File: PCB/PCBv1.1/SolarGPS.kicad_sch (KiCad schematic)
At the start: 54 parts, among them J1 Conn_01x10_Female, J2 Solar1+, J3 GND, J4 Conn_02x05_Odd_Even, J5 Solar2+, J6 GND, J7 Screw_Terminal_01x01, U2 MAX-M10Q, U4 STM32WB5MMGH6TR, U5 BQ25505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

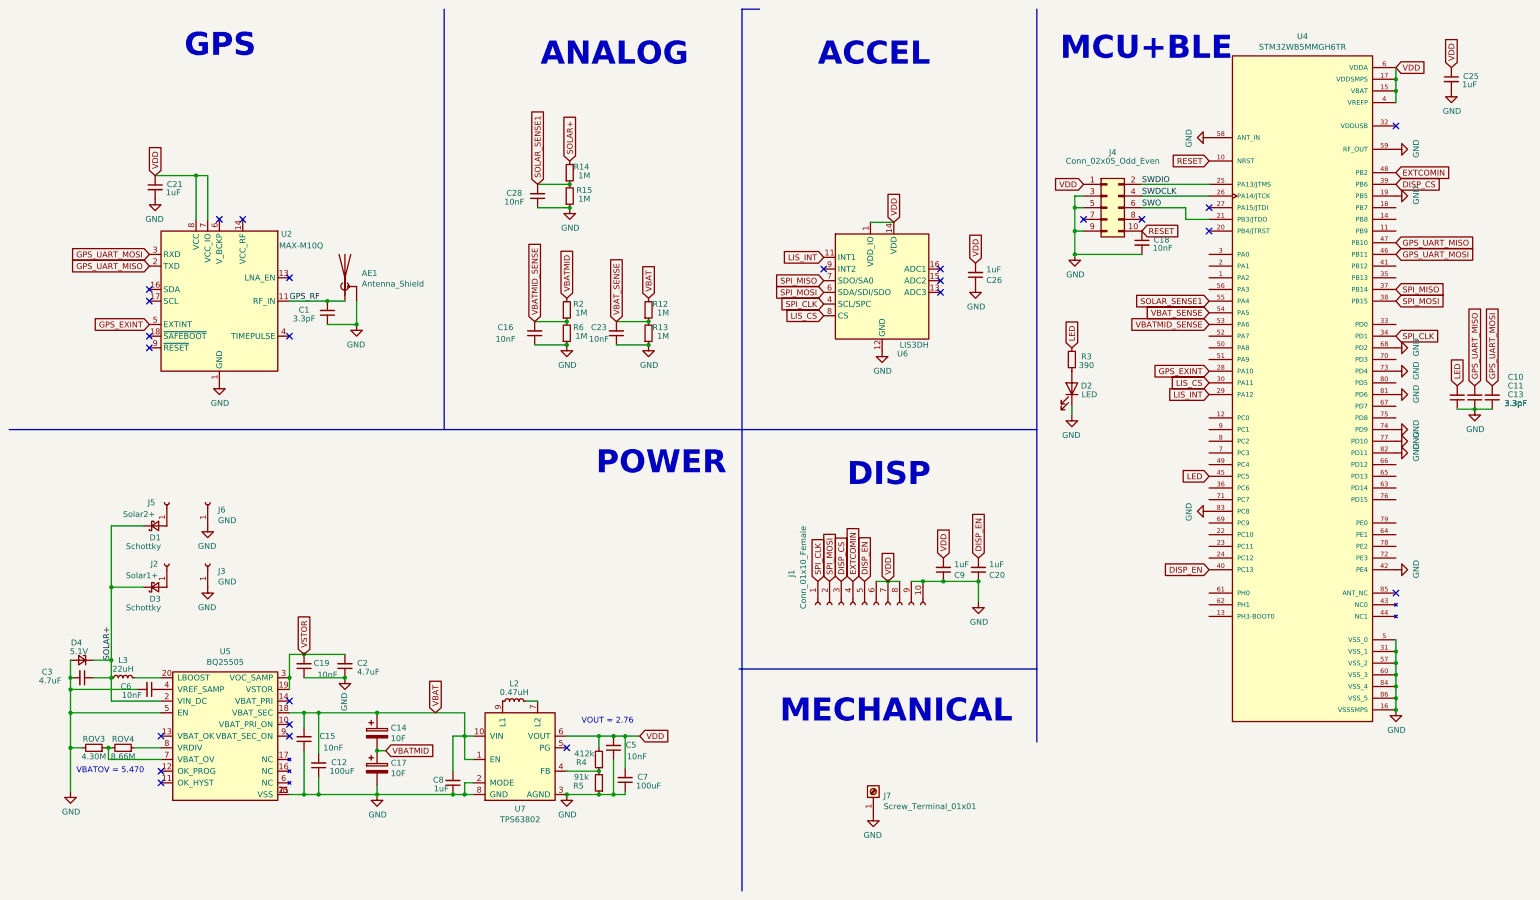
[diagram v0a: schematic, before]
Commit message: Add more App, DropBLE
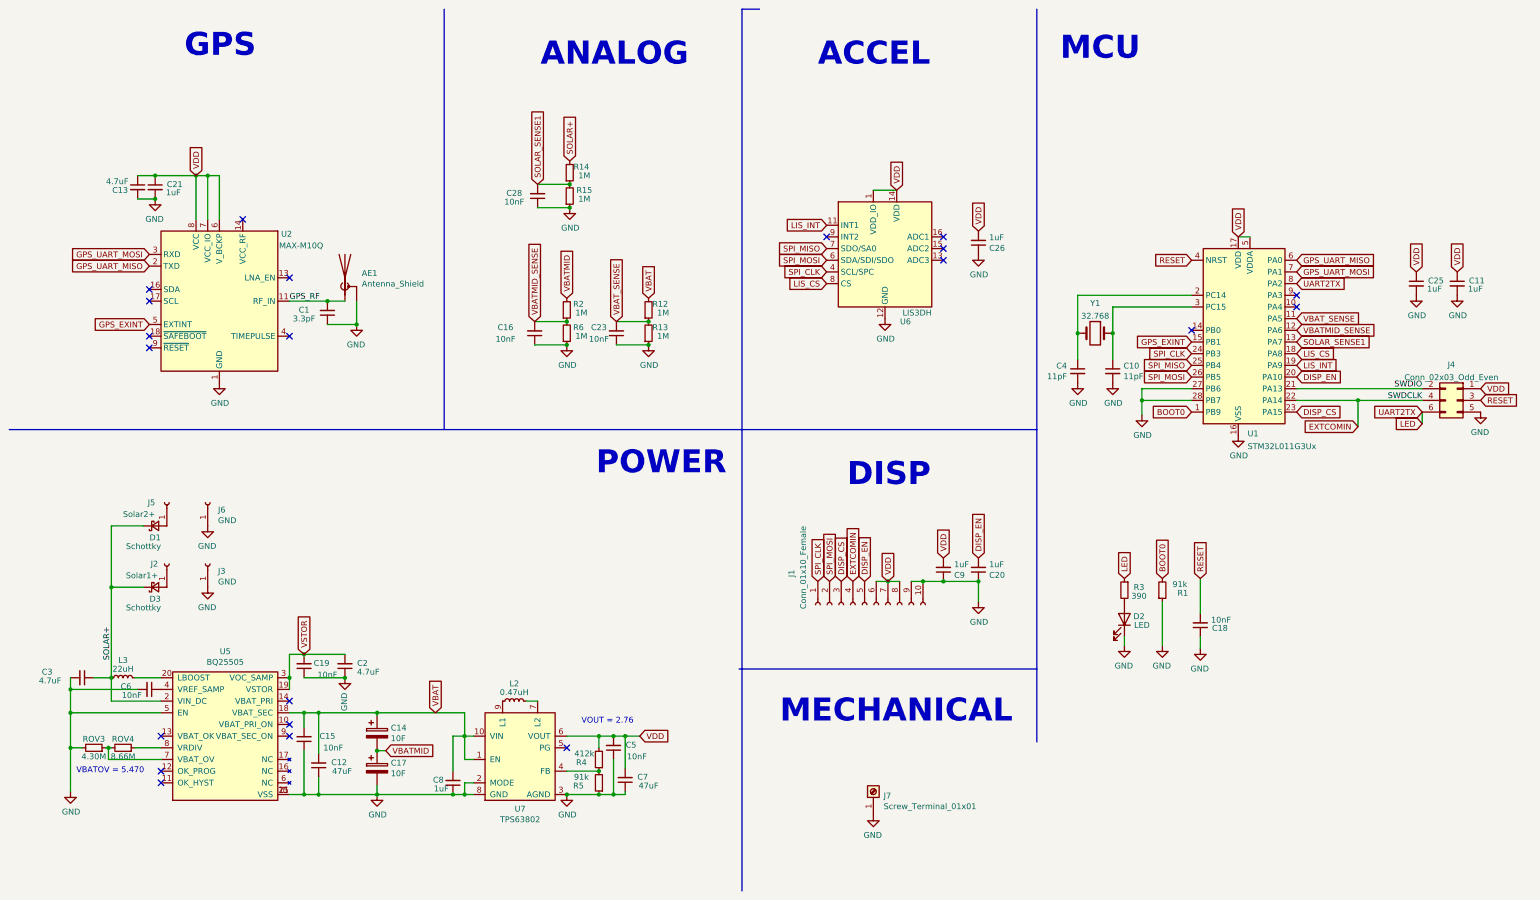
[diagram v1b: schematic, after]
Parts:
- removed D4: 5.1V, Diode_SMD:D_SOD-523, symbol Device:D_Zener_Small
- removed J4: Conn_02x05_Odd_Even, Connector_PinHeader_2.00mm:PinHeader_2x05_P2.00mm_Vertical_SMD, symbol Connector_Generic:Conn_02x05_Odd_Even
- removed U4: STM32WB5MMGH6TR, Veridian-Library-KiCad:XCVR_STM32WB5MMGH6TR, symbol SolarGPS-rescue:STM32WB5MMGH6TR-VeridianDesigns
- added C4: 11pF, Capacitor_SMD:C_0603_1608Metric, symbol Device:C_Small
- added J4: Conn_02x03_Odd_Even, Connector:Tag-Connect_TC2030-IDC-NL_2x03_P1.27mm_Vertical, symbol Connector_Generic:Conn_02x03_Odd_Even
- added R1: 91k, Resistor_SMD:R_0603_1608Metric, symbol Device:R_Small
- added U1: STM32L011G3Ux, Package_DFN_QFN:QFN-28_4x4mm_P0.5mm, symbol MCU_ST_STM32L0:STM32L011G3Ux
- added Y1: 32.768, Crystal:Crystal_SMD_3215-2Pin_3.2x1.5mm, symbol Device:Crystal
- C10: value 3.3pF -> 11pF; footprint Capacitor_SMD:C_0402_1005Metric -> Capacitor_SMD:C_0603_1608Metric
- C11: value 3.3pF -> 1uF; footprint Capacitor_SMD:C_0402_1005Metric -> Capacitor_SMD:C_0603_1608Metric
- C12, C7: value 100uF -> 47uF; footprint Capacitor_SMD:C_1206_3216Metric -> Capacitor_SMD:C_0805_2012Metric
- C13: value 3.3pF -> 4.7uF; footprint Capacitor_SMD:C_0402_1005Metric -> Capacitor_SMD:C_0805_2012Metric
- J1: footprint Margo_Lib:AYF531035 -> Margo_Lib:LS013B7DH03
- U5: footprint Package_DFN_QFN:QFN-20-1EP_3.5x3.5mm_P0.5mm_EP2x2mm_ThermalVias -> Package_DFN_QFN:QFN-20-1EP_3.5x3.5mm_P0.5mm_EP2x2mm
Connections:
- net DISP_CS: now also U1.23 (PA15)
- net DISP_EN: now also U1.20 (PA10)
- net EXTCOMIN: now also J4.4 (Pin_4), U1.22 (PA14)
- net GND: now also C10.2, C11.2, C13.2, C18.1, C4.2, J4.5 (Pin_5), R1.1, U1.16 (VSS), U1.27 (PB6), U1.28 (PB7); no longer C10.1, C11.1, C13.1, C18.2
- net GPS_EXINT: now also U1.15 (PB1)
- net GPS_UART_MISO: now also U1.6 (PA0); no longer C11.2
- net GPS_UART_MOSI: now also U1.7 (PA1); no longer C13.2
- net LED: now also J4.6 (Pin_6), U1.8 (PA2); no longer C10.2
- net LIS_CS: now also U1.18 (PA8)
- net LIS_INT: now also U1.19 (PA9)
- net RESET: now also C18.2, J4.3 (Pin_3), U1.4 (NRST); no longer C18.1
- net SOLAR_SENSE1: now also U1.13 (PA7)
- net SPI_CLK: now also U1.24 (PB3)
- net SPI_MISO: now also U1.25 (PB4)
- net SPI_MOSI: now also U1.26 (PB5)
- net SWDIO: now also J4.2 (Pin_2), U1.21 (PA13)
- net VBATMID_SENSE: now also U1.12 (PA6)
- net VBAT_SENSE: now also U1.11 (PA5)
- net VDD: now also C11.1, C13.1, U2.6 (V_BCKP), J4.1 (Pin_1), U1.17 (VDD), U1.5 (VDDA)
- new net: C4.1, U1.2 (PC14), Y1.2
- new net: C10.1, U1.3 (PC15), Y1.1
- new net BOOT0: R1.2, U1.1 (PB9)
- no-connect marks 25 -> 21
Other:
- note added: "MCU"
- note removed: "MCU+BLE"
- moved on the sheet: C18, C25, C26, D2, R3, U6

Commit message: Add some datasheets
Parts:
- R4: value 412k -> 432k
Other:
- note added: "VOUT = 2.87"
- note removed: "VOUT = 2.76"
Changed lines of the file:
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@@
   (no_connect (at 215.265 66.675))
   (no_connect (at 45.085 177.8))
+  (no_connect (at 292.1 76.835))
   (no_connect (at 215.265 64.135))
   (no_connect (at 292.1 74.295))
-  (no_connect (at 292.1 76.835))
   (no_connect (at 73.025 167.64))
   (no_connect (at 269.24 81.915))
   (no_connect (at 189.865 61.595))
-  (no_connect (at 133.35 172.72))
   (no_connect (at 73.025 170.18))
   (no_connect (at 215.265 61.595))
+  (no_connect (at 133.35 172.72))
   (no_connect (at 42.545 85.725))
   (no_connect (at 42.545 73.025))
@@
     (stroke (width 0) (type default) (color 0 0 0 0))
   )
-  (text "VOUT = 2.76" (at 136.525 167.64 0)
+  (text "VOUT = 2.87" (at 136.525 167.64 0)
     (effects (font (size 1.27 1.27)) (justify left bottom))
   )
@@
     (in_bom yes) (on_board yes)
     (property "Reference" "R4" (id 0) (at 136.525 175.895 0))
-    (property "Value" "412k" (id 1) (at 137.16 173.99 0))
+    (property "Value" "432k" (id 1) (at 137.16 173.99 0))
     (property "Footprint" "Resistor_SMD:R_0603_1608Metric" (id 2) (at 140.335 175.26 0)
       (effects (font (size 1.27 1.27)) hide)
@@
     )
     (path "/00000000-0000-0000-0000-000061ac0081"
-      (reference "R4") (unit 1) (value "412k") (footprint "Resistor_SMD:R_0603_1608Metric")
+      (reference "R4") (unit 1) (value "432k") (footprint "Resistor_SMD:R_0603_1608Metric")
     )
     (path "/00000000-0000-0000-0000-000061ae367a"

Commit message: Add custom library revise M4 mount
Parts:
- J7: footprint Veridian-Library-KiCad:Right Angle Screw Terminal M3M4 -> Heliograph:M4_RA_7792; Part 7781 -> 7792
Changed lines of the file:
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@@
       (effects (font (size 1.27 1.27)) (justify right))
     )
-    (property "Footprint" "Veridian-Library-KiCad:Right Angle Screw Terminal M3M4" (id 2) (at 200.025 182.245 0)
+    (property "Footprint" "Heliograph:M4_RA_7792" (id 2) (at 200.025 182.245 0)
       (effects (font (size 1.27 1.27)) hide)
     )
@@
       (effects (font (size 1.27 1.27)) hide)
     )
-    (property "Part" "7781" (id 4) (at 200.025 182.245 90)
+    (property "Part" "7792" (id 4) (at 200.025 182.245 90)
       (effects (font (size 1.27 1.27)) hide)
     )
@@
     )
     (path "/00000000-0000-0000-0000-000061db9c44"
-      (reference "J7") (unit 1) (value "Screw_Terminal_01x01") (footprint "Veridian-Library-KiCad:Right Angle Screw Terminal M3M4")
+      (reference "J7") (unit 1) (value "Screw_Terminal_01x01") (footprint "Heliograph:M4_RA_7792")
     )
     (path "/00000000-0000-0000-0000-000061a9953b"

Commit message: Update PCB 1.1
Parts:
- C12, C7: footprint Capacitor_SMD:C_0805_2012Metric -> Capacitor_SMD:C_1206_3216Metric
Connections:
- net GND: no longer U1.28 (PB7)
- no-connect marks 21 -> 22
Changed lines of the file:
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@@
   (junction (at 43.815 53.34) (diameter 0) (color 0 0 0 0)
-  )
-  (junction (at 258.445 97.155) (diameter 0) (color 0 0 0 0)
   )
   (junction (at 76.2 182.88) (diameter 0) (color 0 0 0 0)
@@
   (no_connect (at 215.265 64.135))
   (no_connect (at 292.1 74.295))
+  (no_connect (at 269.24 97.155))
   (no_connect (at 73.025 167.64))
   (no_connect (at 269.24 81.915))
@@
     (stroke (width 0) (type default) (color 0 0 0 0))
   )
-  (wire (pts (xy 269.24 97.155) (xy 258.445 97.155))
-    (stroke (width 0) (type default) (color 0 0 0 0))
-  )
   (wire (pts (xy 111.125 182.88) (xy 113.03 182.88))
     (stroke (width 0) (type default) (color 0 0 0 0))
@@
     (stroke (width 0) (type default) (color 0 0 0 0))
   )
-  (wire (pts (xy 258.445 97.155) (xy 258.445 100.33))
-    (stroke (width 0) (type default) (color 0 0 0 0))
-  )
   (wire (pts (xy 76.2 165.1) (xy 76.2 168.275))
     (stroke (width 0) (type default) (color 0 0 0 0))
@@
     (stroke (width 0) (type default) (color 0 0 0 0))
   )
-  (wire (pts (xy 258.445 94.615) (xy 258.445 97.155))
+  (wire (pts (xy 258.445 94.615) (xy 258.445 100.33))
     (stroke (width 0) (type default) (color 0 0 0 0))
   )
@@
     (property "Reference" "C12" (id 0) (at 83.82 175.895 0))
     (property "Value" "47uF" (id 1) (at 84.455 177.8 0))
-    (property "Footprint" "Capacitor_SMD:C_0805_2012Metric" (id 2) (at 79.375 176.53 0)
+    (property "Footprint" "Capacitor_SMD:C_1206_3216Metric" (id 2) (at 79.375 176.53 0)
       (effects (font (size 1.27 1.27)) hide)
     )
@@
     (property "Reference" "C7" (id 0) (at 149.86 179.07 0))
     (property "Value" "47uF" (id 1) (at 151.13 180.975 0))
-    (property "Footprint" "Capacitor_SMD:C_0805_2012Metric" (id 2) (at 146.05 179.705 0)
+    (property "Footprint" "Capacitor_SMD:C_1206_3216Metric" (id 2) (at 146.05 179.705 0)
       (effects (font (size 1.27 1.27)) hide)
     )
@@
     )
     (path "/00000000-0000-0000-0000-000061af5036"
-      (reference "C7") (unit 1) (value "47uF") (footprint "Capacitor_SMD:C_0805_2012Metric")
+      (reference "C7") (unit 1) (value "47uF") (footprint "Capacitor_SMD:C_1206_3216Metric")
     )
     (path "/00000000-0000-0000-0000-000061ba52ab"
@@
     )
     (path "/00000000-0000-0000-0000-000061957471"
-      (reference "C12") (unit 1) (value "47uF") (footprint "Capacitor_SMD:C_0805_2012Metric")
+      (reference "C12") (unit 1) (value "47uF") (footprint "Capacitor_SMD:C_1206_3216Metric")
     )
     (path "/9b88f61c-18a3-402d-bc49-08320c270f61"

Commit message: Tweak PCB
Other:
- moved on the sheet: C10, C4, Y1
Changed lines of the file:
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@@
   (junction (at 76.2 165.1) (diameter 0) (color 0 0 0 0)
   )
-  (junction (at 244.475 82.55) (diameter 0) (color 0 0 0 0)
-  )
   (junction (at 25.4 160.02) (diameter 0) (color 0 0 0 0)
   )
@@
   (junction (at 43.815 48.26) (diameter 0) (color 0 0 0 0)
   )
+  (junction (at 252.095 77.47) (diameter 0) (color 0 0 0 0)
+  )
   (junction (at 55.245 48.26) (diameter 0) (color 0 0 0 0)
   )
   (junction (at 140.335 177.8) (diameter 0) (color 0 0 0 0)
   )
+  (junction (at 244.475 77.47) (diameter 0) (color 0 0 0 0)
+  )
   (junction (at 203.2 136.525) (diameter 0) (color 0 0 0 0)
   )
@@
   )
   (junction (at 87.63 80.645) (diameter 0) (color 0 0 0 0)
-  )
-  (junction (at 252.095 82.55) (diameter 0) (color 0 0 0 0)
   )
   (junction (at 34.29 157.48) (diameter 0) (color 0 0 0 0)
@@
     (stroke (width 0) (type default) (color 0 0 0 0))
   )
-  (wire (pts (xy 244.475 88.265) (xy 244.475 82.55))
-    (stroke (width 0) (type default) (color 0 0 0 0))
-  )
   (wire (pts (xy 52.705 48.26) (xy 55.245 48.26))
     (stroke (width 0) (type default) (color 0 0 0 0))
@@
     (stroke (width 0) (type default) (color 0 0 0 0))
   )
-  (wire (pts (xy 244.475 74.295) (xy 244.475 82.55))
-    (stroke (width 0) (type default) (color 0 0 0 0))
-  )
   (wire (pts (xy 52.705 48.26) (xy 43.815 48.26))
     (stroke (width 0) (type default) (color 0 0 0 0))
@@
     (stroke (width 0) (type default) (color 0 0 0 0))
   )
+  (wire (pts (xy 244.475 74.295) (xy 244.475 77.47))
+    (stroke (width 0) (type default) (color 0 0 0 0))
+  )
   (wire (pts (xy 258.445 94.615) (xy 269.24 94.615))
     (stroke (width 0) (type default) (color 0 0 0 0))
@@
     (stroke (width 0) (type default) (color 0 0 0 0))
   )
+  (wire (pts (xy 252.095 77.47) (xy 252.095 80.01))
+    (stroke (width 0) (type default) (color 0 0 0 0))
+  )
   (wire (pts (xy 92.075 182.88) (xy 108.585 182.88))
     (stroke (width 0) (type default) (color 0 0 0 0))
@@
     (stroke (width 0) (type default) (color 0 0 0 0))
   )
-  (wire (pts (xy 252.095 82.55) (xy 252.095 76.835))
+  (wire (pts (xy 252.095 76.835) (xy 252.095 77.47))
     (stroke (width 0) (type default) (color 0 0 0 0))
   )
@@
     (stroke (width 0) (type default) (color 0 0 0 0))
   )
-  (wire (pts (xy 252.095 88.265) (xy 252.095 82.55))
+  (wire (pts (xy 244.475 77.47) (xy 244.475 80.01))
     (stroke (width 0) (type default) (color 0 0 0 0))
   )
@@
     (pin "2")
   )
-  (symbol (lib_id "power:GND") (at 252.095 93.345 0) (unit 1)
-    (in_bom yes) (on_board yes)
-    (property "Reference" "#PWR0110" (id 0) (at 252.095 99.695 0)
-      (effects (font (size 1.27 1.27)) hide)
-    )
-    (property "Value" "GND" (id 1) (at 252.222 97.7392 0))
-    (property "Footprint" "" (id 2) (at 252.095 93.345 0)
-      (effects (font (size 1.27 1.27)) hide)
-    )
-    (property "Datasheet" "" (id 3) (at 252.095 93.345 0)
-      (effects (font (size 1.27 1.27)) hide)
-    )
-    (pin "1")
-  )
-  (symbol (lib_id "Device:C_Small") (at 244.475 90.805 0) (mirror y) (unit 1)
-    (in_bom yes) (on_board yes)
-    (property "Reference" "C4" (id 0) (at 242.1382 89.6366 0)
-      (effects (font (size 1.27 1.27)) (justify left))
-    )
-    (property "Value" "11pF" (id 1) (at 242.1382 91.948 0)
-      (effects (font (size 1.27 1.27)) (justify left))
-    )
-    (property "Footprint" "Capacitor_SMD:C_0603_1608Metric" (id 2) (at 244.475 90.805 0)
-      (effects (font (size 1.27 1.27)) hide)
-    )
-    (property "Datasheet" "~" (id 3) (at 244.475 90.805 0)
-      (effects (font (size 1.27 1.27)) hide)
-    )
-    (pin "1")
-    (pin "2")
-  )
-  (symbol (lib_id "Device:Crystal") (at 248.285 82.55 0) (mirror y) (unit 1)
-    (in_bom yes) (on_board yes) (fields_autoplaced)
-    (property "Reference" "Y1" (id 0) (at 248.285 76.0181 0))
-    (property "Value" "32.768" (id 1) (at 248.285 78.7932 0))
-    (property "Footprint" "Crystal:Crystal_SMD_3215-2Pin_3.2x1.5mm" (id 2) (at 248.285 82.55 0)
-      (effects (font (size 1.27 1.27)) hide)
-    )
-    (property "Datasheet" "~" (id 3) (at 248.285 82.55 0)
-      (effects (font (size 1.27 1.27)) hide)
-    )
-    (property "Part" "SC32S-7PF20PPM" (id 4) (at 248.285 82.55 0)
+  (symbol (lib_id "power:GND") (at 252.095 85.09 0) (unit 1)
+    (in_bom yes) (on_board yes)
+    (property "Reference" "#PWR0110" (id 0) (at 252.095 91.44 0)
+      (effects (font (size 1.27 1.27)) hide)
+    )
+    (property "Value" "GND" (id 1) (at 252.222 89.4842 0))
+    (property "Footprint" "" (id 2) (at 252.095 85.09 0)
+      (effects (font (size 1.27 1.27)) hide)
+    )
+    (property "Datasheet" "" (id 3) (at 252.095 85.09 0)
+      (effects (font (size 1.27 1.27)) hide)
+    )
+    (pin "1")
+  )
+  (symbol (lib_id "Device:C_Small") (at 244.475 82.55 0) (mirror y) (unit 1)
+    (in_bom yes) (on_board yes)
+    (property "Reference" "C4" (id 0) (at 241.3 81.28 0)
+      (effects (font (size 1.27 1.27)) (justify left))
+    )
+    (property "Value" "11pF" (id 1) (at 242.57 83.185 0)
+      (effects (font (size 1.27 1.27)) (justify left))
+    )
+    (property "Footprint" "Capacitor_SMD:C_0603_1608Metric" (id 2) (at 244.475 82.55 0)
+      (effects (font (size 1.27 1.27)) hide)
+    )
+    (property "Datasheet" "~" (id 3) (at 244.475 82.55 0)
+      (effects (font (size 1.27 1.27)) hide)
+    )
+    (pin "1")
+    (pin "2")
+  )
+  (symbol (lib_id "Device:Crystal") (at 248.285 77.47 0) (mirror y) (unit 1)
+    (in_bom yes) (on_board yes)
+    (property "Reference" "Y1" (id 0) (at 248.285 70.9381 0))
+    (property "Value" "32.768" (id 1) (at 248.285 73.025 0))
+    (property "Footprint" "Crystal:Crystal_SMD_3215-2Pin_3.2x1.5mm" (id 2) (at 248.285 77.47 0)
+      (effects (font (size 1.27 1.27)) hide)
+    )
+    (property "Datasheet" "~" (id 3) (at 248.285 77.47 0)
+      (effects (font (size 1.27 1.27)) hide)
+    )
+    (property "Part" "SC32S-7PF20PPM" (id 4) (at 248.285 77.47 0)
       (effects (font (size 1.27 1.27)) hide)
     )
@@
     (pin "2")
   )
-  (symbol (lib_id "Device:C_Small") (at 252.095 90.805 0) (unit 1)
-    (in_bom yes) (on_board yes)
-    (property "Reference" "C10" (id 0) (at 254.4318 89.6366 0)
-      (effects (font (size 1.27 1.27)) (justify left))
-    )
-    (property "Value" "11pF" (id 1) (at 254.4318 91.948 0)
-      (effects (font (size 1.27 1.27)) (justify left))
-    )
-    (property "Footprint" "Capacitor_SMD:C_0603_1608Metric" (id 2) (at 252.095 90.805 0)
-      (effects (font (size 1.27 1.27)) hide)
-    )
-    (property "Datasheet" "~" (id 3) (at 252.095 90.805 0)
+  (symbol (lib_id "Device:C_Small") (at 252.095 82.55 0) (unit 1)
+    (in_bom yes) (on_board yes)
+    (property "Reference" "C10" (id 0) (at 254 80.01 0)
+      (effects (font (size 1.27 1.27)) (justify left))
+    )
+    (property "Value" "11pF" (id 1) (at 254 81.915 0)
+      (effects (font (size 1.27 1.27)) (justify left))
+    )
+    (property "Footprint" "Capacitor_SMD:C_0603_1608Metric" (id 2) (at 252.095 82.55 0)
+      (effects (font (size 1.27 1.27)) hide)
+    )
+    (property "Datasheet" "~" (id 3) (at 252.095 82.55 0)
       (effects (font (size 1.27 1.27)) hide)
     )
@@
     (pin "1")
   )
-  (symbol (lib_id "power:GND") (at 244.475 93.345 0) (unit 1)
-    (in_bom yes) (on_board yes)
-    (property "Reference" "#PWR0108" (id 0) (at 244.475 99.695 0)
-      (effects (font (size 1.27 1.27)) hide)
-    )
-    (property "Value" "GND" (id 1) (at 244.602 97.7392 0))
-    (property "Footprint" "" (id 2) (at 244.475 93.345 0)
-      (effects (font (size 1.27 1.27)) hide)
-    )
-    (property "Datasheet" "" (id 3) (at 244.475 93.345 0)
-      (effects (font (size 1.27 1.27)) hide)
-    )
+  (symbol (lib_id "power:GND") (at 244.475 85.09 0) (unit 1)
+    (in_bom yes) (on_board yes)
+    (property "Reference" "#PWR0108" (id 0) (at 244.475 91.44 0)
+      (effects (font (size 1.27 1.27)) hide)
+    )
+    (property "Value" "GND" (id 1) (at 244.602 89.4842 0))
+    (property "Footprint" "" (id 2) (at 244.475 85.09 0)
+      (effects (font (size 1.27 1.27)) hide)
+    )
+    (property "Datasheet" "" (id 3) (at 244.475 85.09 0)
+      (effects (font (size 1.27 1.27)) hide)
+    )
